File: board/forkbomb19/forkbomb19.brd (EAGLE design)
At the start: 89.2 x 83.7 mm, 75 parts, among them T3 MMUN2133LT1G, U1 ESP-WROOM-03, U4 TPS61090RSAR

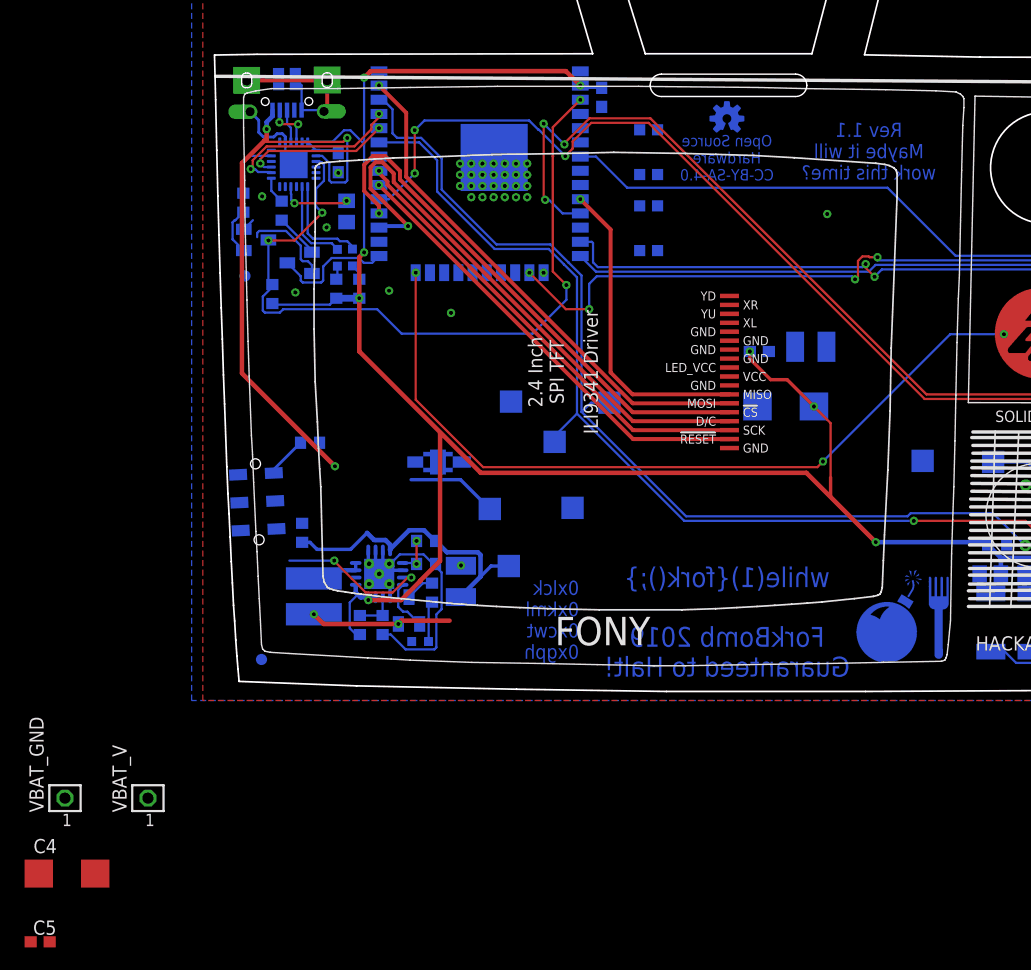
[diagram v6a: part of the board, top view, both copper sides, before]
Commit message: started doing layout for rev 1.1
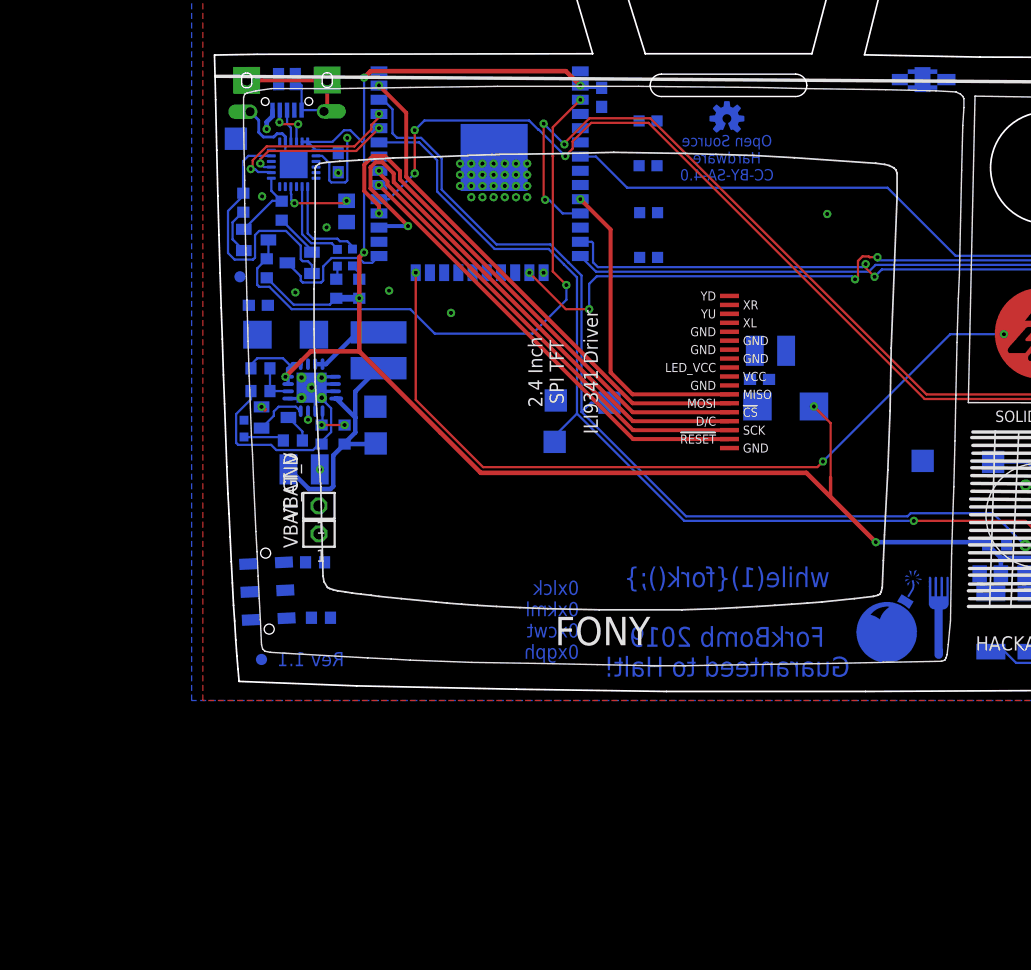
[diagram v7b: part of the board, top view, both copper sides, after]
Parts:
- moved C5 60.2 mm to (4.11, 34.3), flipped to the bottom, turned to 180 degrees
- moved C4 52.0 mm to (6.55, 31.7), flipped to the bottom
- moved TP_PWR_VBUS 40.1 mm to (2.10, 49.2)
- moved VBAT_GND 32.8 mm to (9.53, 13.9)
- moved VBAT_V 30.3 mm to (9.52, 16.4)
- moved LOW_BATT 24.7 mm to (2.83, 23.3), turned to 0 degrees
- moved R19 24.6 mm to (4.30, 28.7), turned to 0 degrees
- moved R21 23.6 mm to (4.30, 26.6), turned to 180 degrees
- moved L1 22.7 mm to (14.9, 30.3)
- moved T3 21.0 mm to (5.59, 24.3), turned to 90 degrees
- moved TP_BATT_GND 19.8 mm to (14.6, 25.2)
- moved R20 18.4 mm to (7.19, 22.2), turned to 180 degrees
- moved U4 17.7 mm to (8.87, 26.9), turned to 270 degrees
- moved C2 17.2 mm to (8.20, 19.6), turned to 180 degrees
- moved TP_BATT_VBAT 16.2 mm to (14.6, 22.0)
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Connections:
- net EN: no longer U3.9
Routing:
- net VBUS: track 60.7 -> 10.5 mm, vias 3 -> 2
- net VBAT: track 42.6 -> 23.8 mm, vias 2 -> 1
- net +3V3: track 237.7 -> 219.3 mm, vias 9 -> 8
- net EN: track 67.3 -> 54.6 mm, vias 4 -> 2
- net ENABLE: track 13.4 -> 1.09 mm, vias 2 -> 1
- net DAT_TERM_RDY: track 13.7 -> 24.2 mm
- net N$13: track 3.38 -> 0.00 mm
- net RDY_2_SND: track 3.59 -> 6.84 mm
- net N$16: track 5.50 -> 6.84 mm
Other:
- board text added: "Rev 1.1"
- board text removed: "Rev 1.1 Maybe it will work this time?"
- board text removed: "VLIPO"

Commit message: finished rev 1.1
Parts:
- removed VBAT_GND, VBAT_V: POT_GND, con-samtec:TSW-101-XX-G-S
- added N1: MCH3484, forkbomb19:MCH3484
- added VBAT+, VBAT-: POT_GND, con-samtec:TSW-101-XX-G-S
- R24: value 1.33M -> 1.13M
- moved FID4 21.6 mm to (4.62, 15.4)
- moved TP_BATT_GND 7.47 mm to (15.2, 17.8)
- moved C5 2.40 mm to (2.63, 36.2), turned to 90 degrees
- moved C1 1.67 mm to (36.1, 54.0), turned to 180 degrees
- moved TP_BATT_VBAT 1.34 mm to (15.2, 20.7)
- moved C13 1.00 mm to (52.3, 25.3)
- moved C14 1.00 mm to (49.9, 27.7)
- moved R14 1.00 mm to (50.9, 30.2)
- moved U$2 1.00 mm to (47.2, 28.3)
- moved R18 0.73 mm to (9.50, 10.7), turned to 270 degrees
- moved HARDRST 0.65 mm to (38.5, 41.0)
- moved C4 0.61 mm to (6.17, 32.2), turned to 180 degrees
- moved R1 0.61 mm to (4.89, 37.0)
- moved SOFTRESET 0.50 mm to (38.5, 49.0)
- moved R9 0.28 mm to (9.44, 6.27), turned to 270 degrees
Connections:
- removed net I2C_GND: TP_I2C_GND.TP
- new net N$18: N1.D, VBAT-.1
- net GND: now also N1.S, TP_I2C_GND.TP; no longer VBAT_GND.1
- net VBAT: now also N1.G, VBAT+.1; no longer VBAT_V.1
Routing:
- net VBAT: track 23.8 -> 53.7 mm, vias 1 -> 2
- net ENABLE: track 1.09 -> 20.1 mm, vias 1 -> 2
- net +3V3: track 219.3 -> 236.5 mm, vias 8 -> 10
- net EN: track 54.6 -> 67.0 mm, vias 2 -> 3
- net VBUS: track 10.5 -> 21.1 mm, vias 2 -> 3
- net N$2: track 0.08 -> 9.69 mm
- net N$18: track 0.00 -> 9.27 mm
- net N$3: track 0.00 -> 7.57 mm, vias 0 -> 2
- net N$13: track 0.00 -> 6.89 mm
- net GND: track 61.1 -> 66.6 mm, vias 40 -> 41
- net N$1: track 0.00 -> 3.48 mm, vias 0 -> 1
- net SCRN_RST: track 40.7 -> 41.7 mm
- net SCRN_MOSI: track 46.5 -> 47.5 mm
- net SCRN_MISO: track 28.0 -> 29.0 mm
- net SCRN_D/CX: track 51.6 -> 52.6 mm
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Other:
- board text added: "frkbmb.dev"
- board text added: "lknorr ctan maxl ghaack"
- board text removed: "0xlck 0xkml 0xcwt 0xgph"
